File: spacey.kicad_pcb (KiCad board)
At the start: 2 copper layers, 129.9 x 111 mm, 16 parts, among them J1 Screw_Terminal_01x02, SW1 SW_Omron_B3FS, SW10 SW_Omron_B3FS, SW2 SW_Omron_B3FS, SW3 SW_Omron_B3FS, SW4 SW_Omron_B3FS, SW5 SW_Omron_B3FS, SW6 SW_Omron_B3FS, SW7 SW_Omron_B3FS, SW8 SW_Omron_B3FS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

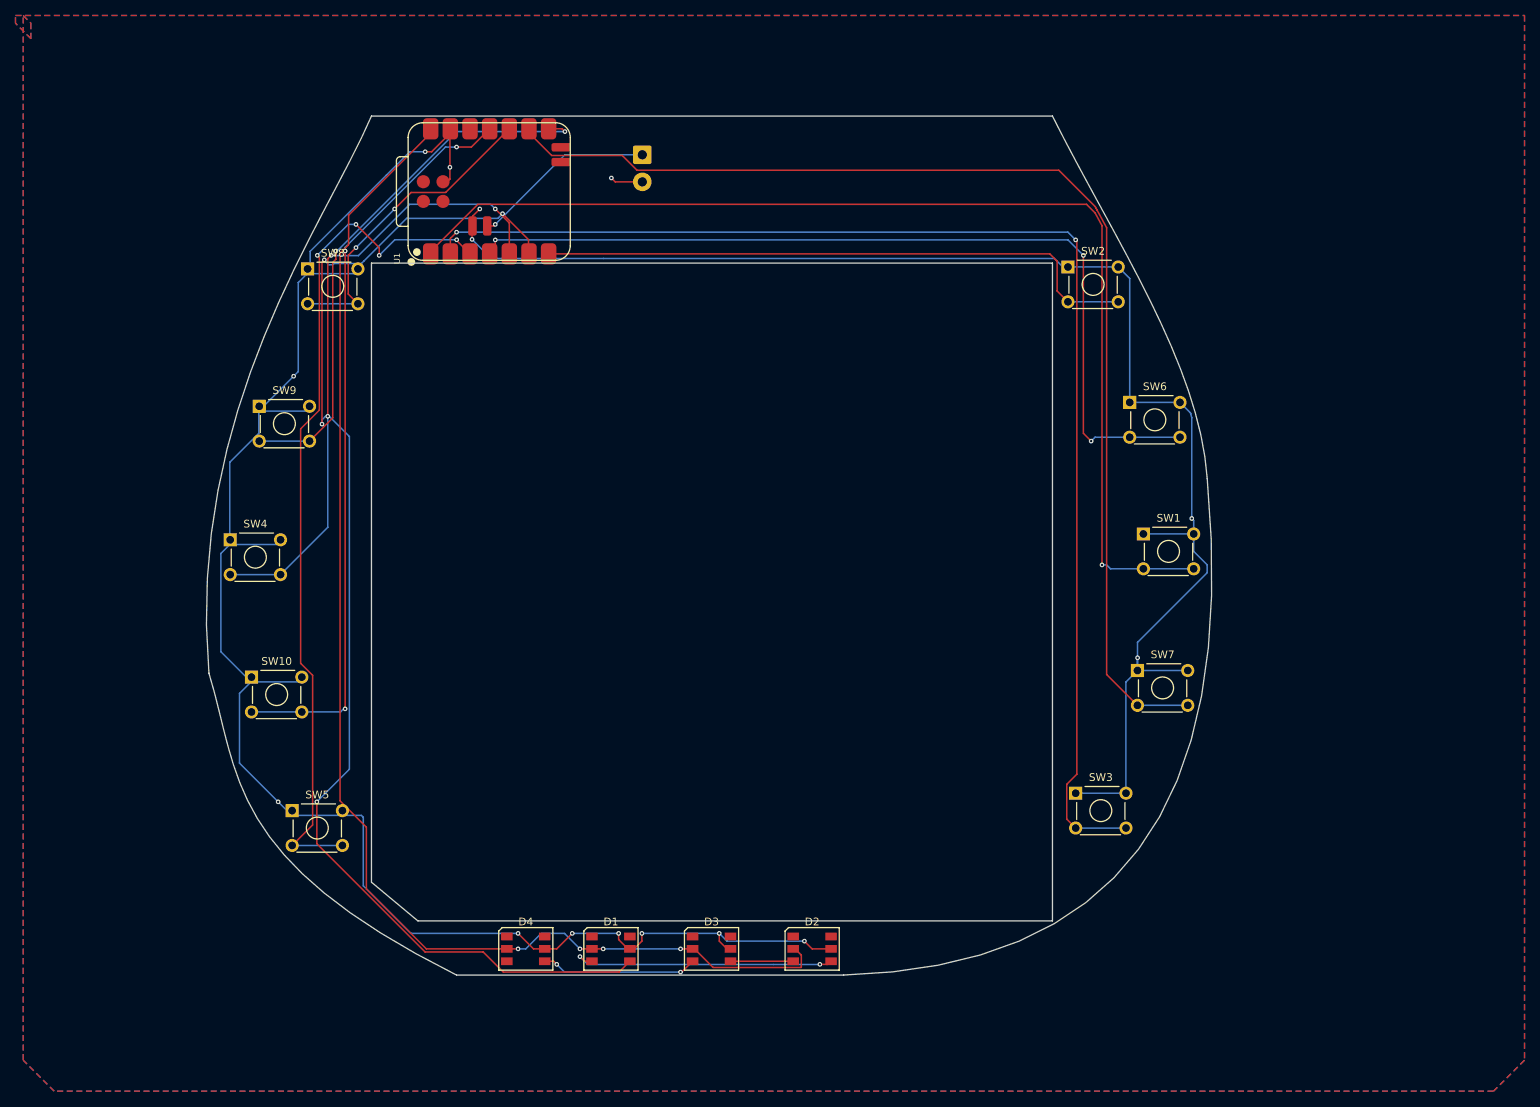
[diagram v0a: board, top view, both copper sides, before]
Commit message: Fixed DRC errors
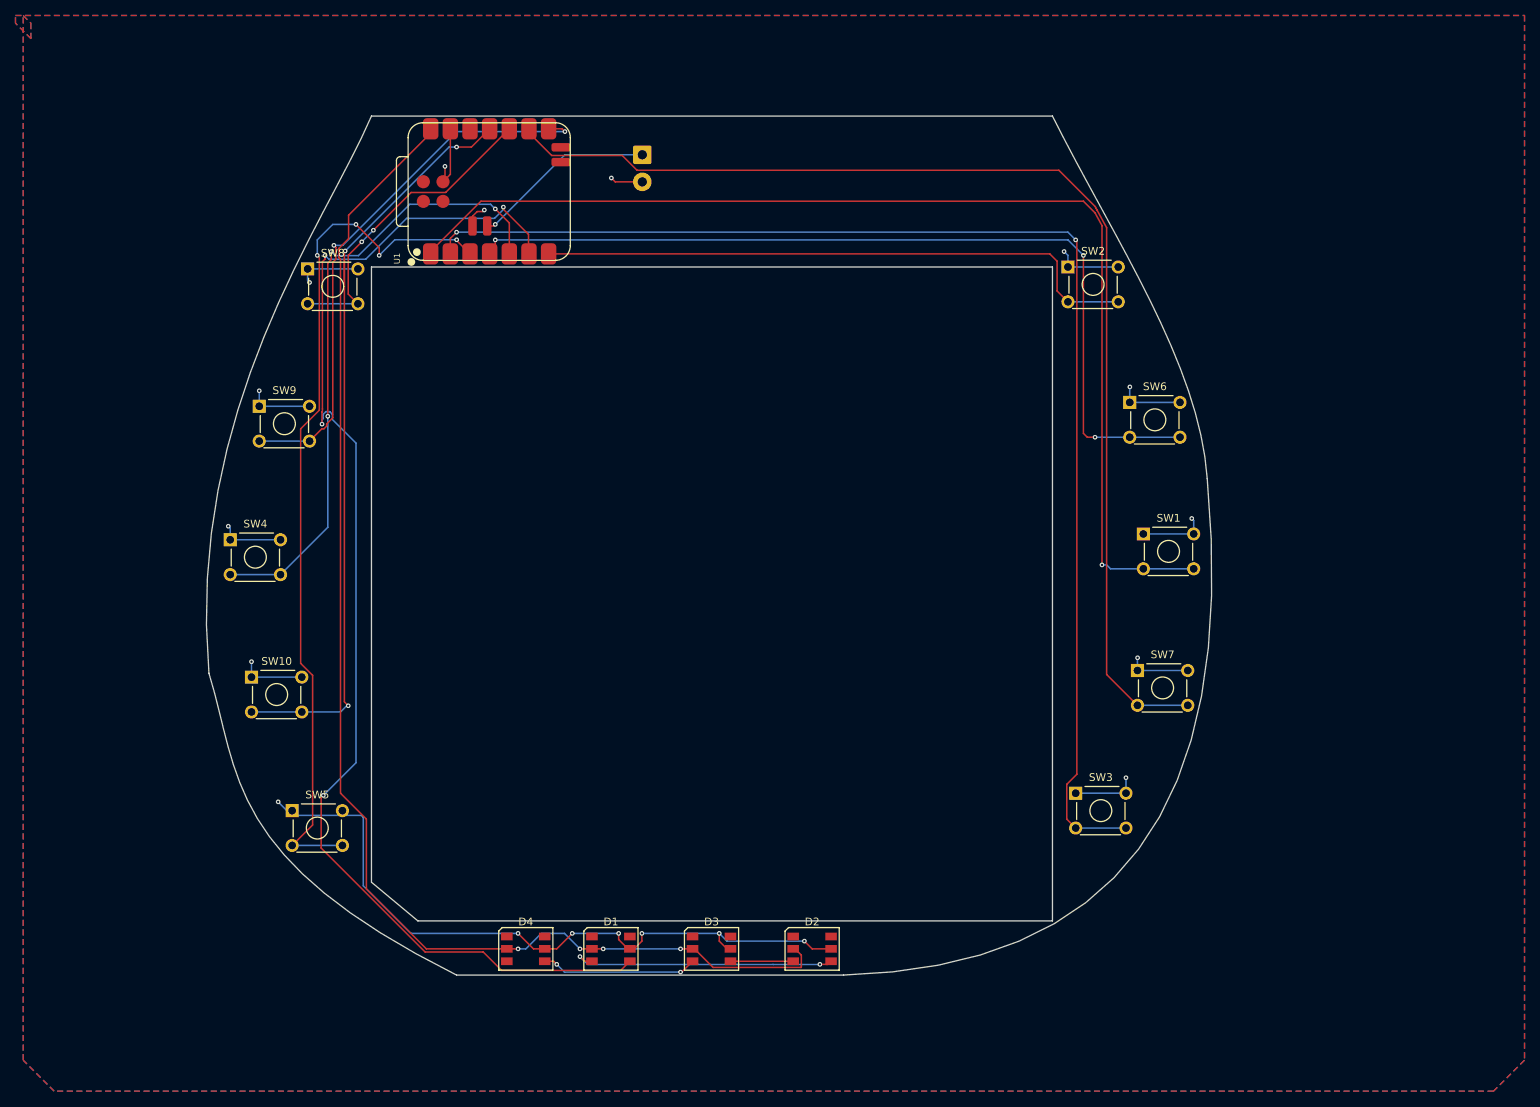
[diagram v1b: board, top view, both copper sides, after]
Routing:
- net GND: track 425.5 -> 184.7 mm, vias 15 -> 19
- net bt_10: track 96.9 -> 101.1 mm
- net DIN: track 162.2 -> 165.5 mm
- net bt_4: track 110.9 -> 112.1 mm
- net bt_7: track 70.7 -> 71.7 mm
- net bt_2: track 81.2 -> 81.9 mm
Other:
- outline, holes or cut-outs redrawn
